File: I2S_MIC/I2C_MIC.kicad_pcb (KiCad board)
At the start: 2 copper layers, 17.3 x 16.5 mm, 12 parts, among them J1 I2S_PMOD

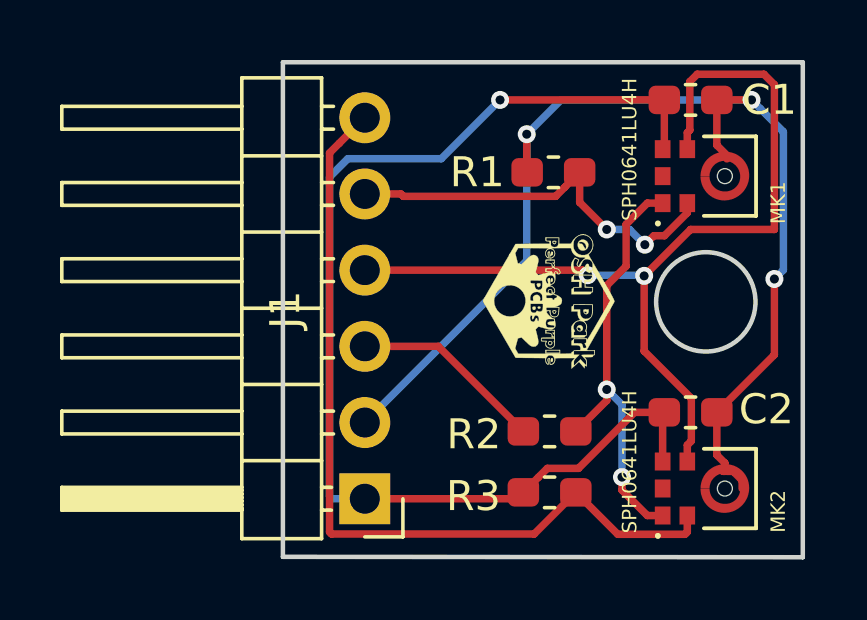
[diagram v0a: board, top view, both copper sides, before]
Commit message: Adding filled zone
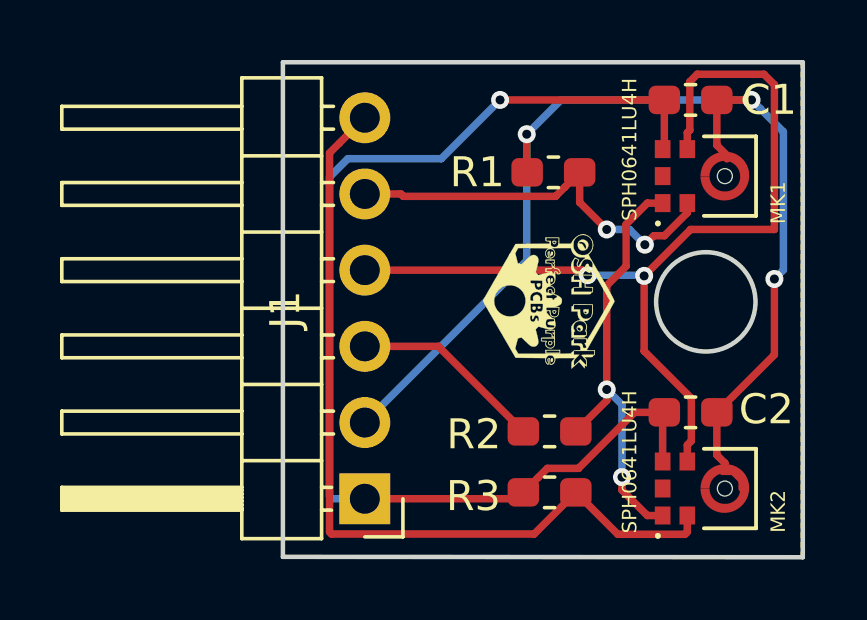
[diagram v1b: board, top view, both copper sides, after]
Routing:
- added copper zone on B.Cu, net GND
- added copper zone on F.Cu, net GND
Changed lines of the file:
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@@
   (segment (start 162.046999 94.225001) (end 155.289999 94.225001) (width 0.25) (layer F.Cu) (net 7))
   (segment (start 163.435 92.837) (end 162.046999 94.225001) (width 0.25) (layer F.Cu) (net 7))
+  (zone (net 2) (net_name GND) (layer F.Cu) (hatch edge 0.508)
+    (connect_pads (clearance 0.508))
+    (min_thickness 0.254)
+    (fill yes (arc_segments 32) (thermal_gap 0.508) (thermal_bridge_width 0.508))
+    (polygon
+      (pts
+        (xy 153.67 78.486) (xy 170.942 78.486) (xy 170.942 94.996) (xy 153.67 94.996)
+      )
+    )
+  )
+  (zone (net 2) (net_name GND) (layer B.Cu) (hatch edge 0.508)
+    (connect_pads (clearance 0.508))
+    (min_thickness 0.254)
+    (fill yes (arc_segments 32) (thermal_gap 0.508) (thermal_bridge_width 0.508))
+    (polygon
+      (pts
+        (xy 153.67 78.486) (xy 170.942 78.486) (xy 170.942 94.996) (xy 153.67 94.996)
+      )
+    )
+  )
 )
